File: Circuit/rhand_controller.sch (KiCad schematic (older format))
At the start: 18 parts, among them P1 BLUETOOTH, SW1 EmSW, SW2 SWITCH_INV, U1 IM315TRX, U2 STM32F042

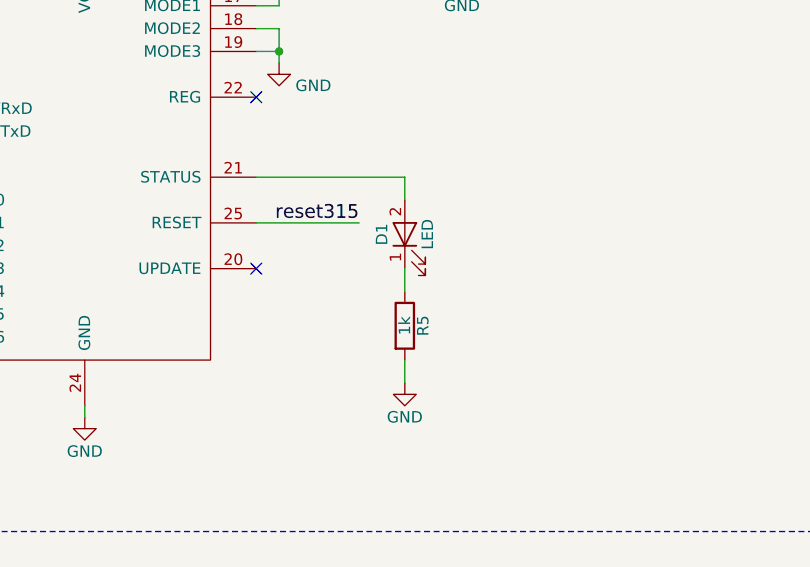
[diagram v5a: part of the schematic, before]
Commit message: IM315のLEDの配線変更
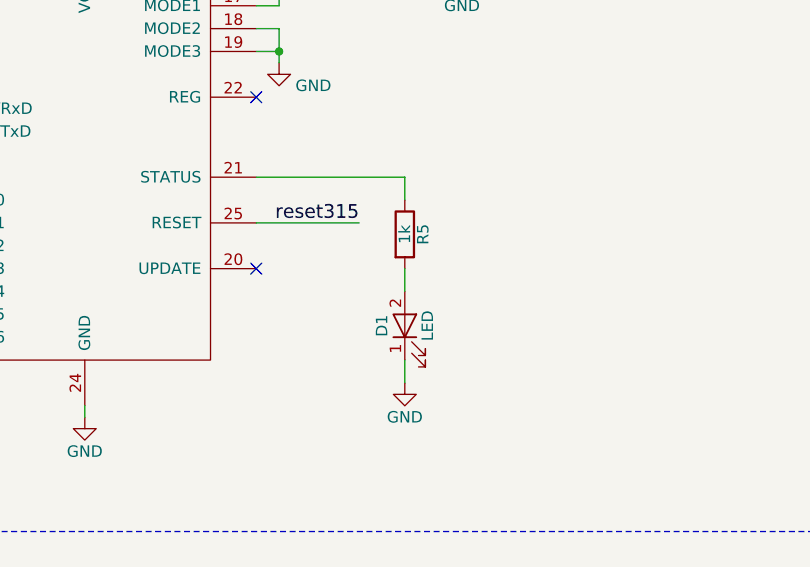
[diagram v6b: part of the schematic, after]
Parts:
- R5: footprint Resistors_SMD:R_0603_HandSoldering -> Resistors_THT:R_Axial_DIN0207_L6.3mm_D2.5mm_P7.62mm_Horizontal
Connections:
- net GND: now also D1.1 (K); no longer R5.2
- net at R5.1: now also U1.21 (STATUS); no longer D1.1 (K)
- net at D1.2 (A): now also R5.2; no longer U1.21 (STATUS)
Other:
- moved on the sheet: D1, R5
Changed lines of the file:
@@
 LIBS:contrib
 LIBS:valves
+LIBS:YASU
 LIBS:device
-LIBS:robocon_sch
 LIBS:rhand_controller-cache
 EELAYER 25 0
@@
 L R R5
 U 1 1 5938D995
-P 3600 3100
-F 0 "R5" V 3680 3100 50  0000 C CNN
-F 1 "1k" V 3600 3100 50  0000 C CNN
-F 2 "Resistors_SMD:R_0603_HandSoldering" V 3530 3100 50  0001 C CNN
-F 3 "" H 3600 3100 50  0001 C CNN
-	1    3600 3100
+P 3600 2700
+F 0 "R5" V 3680 2700 50  0000 C CNN
+F 1 "1k" V 3600 2700 50  0000 C CNN
+F 2 "Resistors_THT:R_Axial_DIN0207_L6.3mm_D2.5mm_P7.62mm_Horizontal" V 3530 2700 50  0001 C CNN
+F 3 "" H 3600 2700 50  0001 C CNN
+	1    3600 2700
 	1    0    0    -1
 $EndComp
@@
 L LED D1
 U 1 1 59426E1D
-P 3600 2700
-F 0 "D1" H 3600 2800 50  0000 C CNN
-F 1 "LED" H 3600 2600 50  0000 C CNN
-F 2 "LEDs:LED_D5.0mm" H 3600 2700 50  0001 C CNN
-F 3 "" H 3600 2700 50  0001 C CNN
-	1    3600 2700
+P 3600 3100
+F 0 "D1" H 3600 3200 50  0000 C CNN
+F 1 "LED" H 3600 3000 50  0000 C CNN
+F 2 "LEDs:LED_D5.0mm" H 3600 3100 50  0001 C CNN
+F 3 "" H 3600 3100 50  0001 C CNN
+	1    3600 3100
 	0    -1   -1   0
 $EndComp
